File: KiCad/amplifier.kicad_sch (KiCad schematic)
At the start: 0 parts

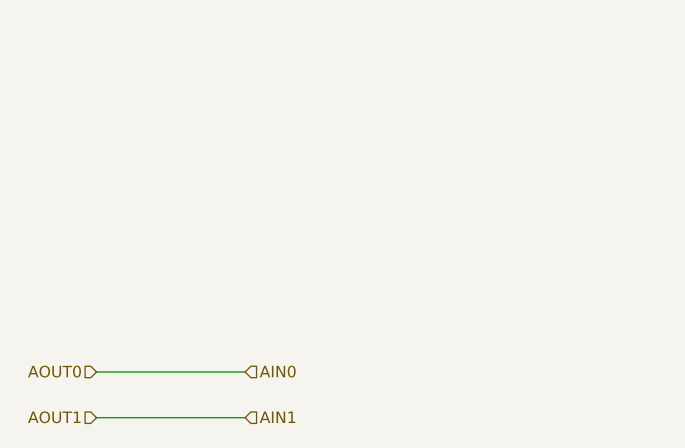
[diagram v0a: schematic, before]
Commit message: Add MCP6V92 Amplifier
Add amplifier part to amplifier block
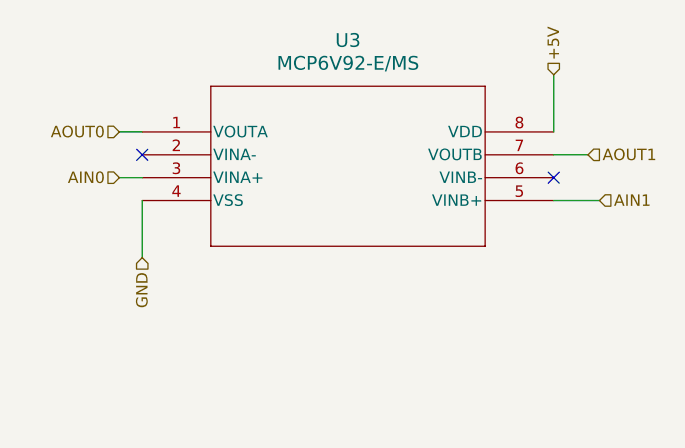
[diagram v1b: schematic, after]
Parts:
- added U3: MCP6V92-E/MS, MSOP8_MS_MCH, symbol Amplifier_Difference:MCP6V92-E_MS
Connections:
- net AIN0: now also U3.3 (VINA+)
- net AIN1: now also U3.5 (VINB+)
- new net +5V: U3.8 (VDD)
- new net AOUT0: U3.1 (VOUTA)
- new net AOUT1: U3.7 (VOUTB)
- new net GND: U3.4 (VSS)
- no-connect marks 0 -> 2
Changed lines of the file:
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@@
 	(generator_version "8.0")
 	(paper "A4")
-	(wire
-		(pts
-			(xy 102.87 95.25) (xy 119.38 95.25)
-		)
-		(stroke
-			(width 0)
-			(type default)
-		)
-	)
-	(wire
-		(pts
-			(xy 102.87 90.17) (xy 119.38 90.17)
+	(no_connect
+		(at 153.67 68.58)
+	)
+	(no_connect
+		(at 107.95 66.04)
+	)
+	(wire
+		(pts
+			(xy 107.95 77.47) (xy 107.95 71.12)
+		)
+		(stroke
+			(width 0)
+			(type default)
+		)
+	)
+	(wire
+		(pts
+			(xy 105.41 68.58) (xy 107.95 68.58)
+		)
+		(stroke
+			(width 0)
+			(type default)
+		)
+	)
+	(wire
+		(pts
+			(xy 105.41 63.5) (xy 107.95 63.5)
+		)
+		(stroke
+			(width 0)
+			(type default)
+		)
+	)
+	(wire
+		(pts
+			(xy 158.75 71.12) (xy 153.67 71.12)
+		)
+		(stroke
+			(width 0)
+			(type default)
+		)
+	)
+	(wire
+		(pts
+			(xy 153.67 57.15) (xy 153.67 63.5)
+		)
+		(stroke
+			(width 0)
+			(type default)
+		)
+	)
+	(wire
+		(pts
+			(xy 157.48 66.04) (xy 153.67 66.04)
 		)
 		(stroke
@@
 	(hierarchical_label "AIN1"
 		(shape input)
-		(at 119.38 95.25 0)
+		(at 158.75 71.12 0)
 		(fields_autoplaced yes)
 		(effects
@@
 		)
 	)
+	(hierarchical_label "+5V"
+		(shape input)
+		(at 153.67 57.15 90)
+		(fields_autoplaced yes)
+		(effects
+			(font
+				(size 1.27 1.27)
+			)
+			(justify left)
+		)
+	)
 	(hierarchical_label "AIN0"
 		(shape input)
-		(at 119.38 90.17 0)
+		(at 105.41 68.58 180)
+		(fields_autoplaced yes)
+		(effects
+			(font
+				(size 1.27 1.27)
+			)
+			(justify right)
+		)
+	)
+	(hierarchical_label "GND"
+		(shape input)
+		(at 107.95 77.47 270)
+		(fields_autoplaced yes)
+		(effects
+			(font
+				(size 1.27 1.27)
+			)
+			(justify right)
+		)
+	)
+	(hierarchical_label "AOUT0"
+		(shape input)
+		(at 105.41 63.5 180)
+		(fields_autoplaced yes)
+		(effects
+			(font
+				(size 1.27 1.27)
+			)
+			(justify right)
+		)
+	)
+	(hierarchical_label "AOUT1"
+		(shape input)
+		(at 157.48 66.04 0)
 		(fields_autoplaced yes)
 		(effects
@@
 		)
 	)
-	(hierarchical_label "AOUT0"
-		(shape input)
-		(at 102.87 90.17 180)
-		(fields_autoplaced yes)
-		(effects
-			(font
-				(size 1.27 1.27)
-			)
-			(justify right)
-		)
-	)
-	(hierarchical_label "AOUT1"
-		(shape input)
-		(at 102.87 95.25 180)
-		(fields_autoplaced yes)
-		(effects
-			(font
-				(size 1.27 1.27)
-			)
-			(justify right)
-		)
-	)
+	(symbol
+		(lib_id "Amplifier_Difference:MCP6V92-E_MS")
+		(at 107.95 63.5 0)
+		(unit 1)
+		(exclude_from_sim no)
+		(in_bom yes)
+		(on_board yes)
+		(dnp no)
+		(fields_autoplaced yes)
+		(property "Reference" "U3"
+			(at 130.81 53.34 0)
+			(effects
+				(font
+					(size 1.524 1.524)
+				)
+			)
+		)
+		(property "Value" "MCP6V92-E/MS"
+			(at 130.81 55.88 0)
+			(effects
+				(font
+					(size 1.524 1.524)
+				)
+			)
+		)
+		(property "Footprint" "MSOP8_MS_MCH"
+			(at 107.95 63.5 0)
+			(effects
+				(font
+					(size 1.27 1.27)
+					(italic yes)
+				)
+				(hide yes)
+			)
+		)
+		(property "Datasheet" "MCP6V92-E/MS"
+			(at 107.95 63.5 0)
+			(effects
+				(font
+					(size 1.27 1.27)
+					(italic yes)
+				)
+				(hide yes)
+			)
+		)
+		(property "Description" ""
+			(at 107.95 63.5 0)
+			(effects
+				(font
+					(size 1.27 1.27)
+				)
+				(hide yes)
+			)
+		)
+		(pin "1"
+		)
+		(pin "5"
+		)
+		(pin "6"
+		)
+		(pin "2"
+		)
+		(pin "7"
+		)
+		(pin "8"
+		)
+		(pin "3"
+		)
+		(pin "4"
+		)
+		(instances
+			(project ""
+				(path "/5d164854-6659-4076-ba4e-df0771b4723d/0ca0ce53-f671-4079-bef4-c51bb5c4b2f4"
+					(reference "U3")
+					(unit 1)
+				)
+			)
+		)
+	)

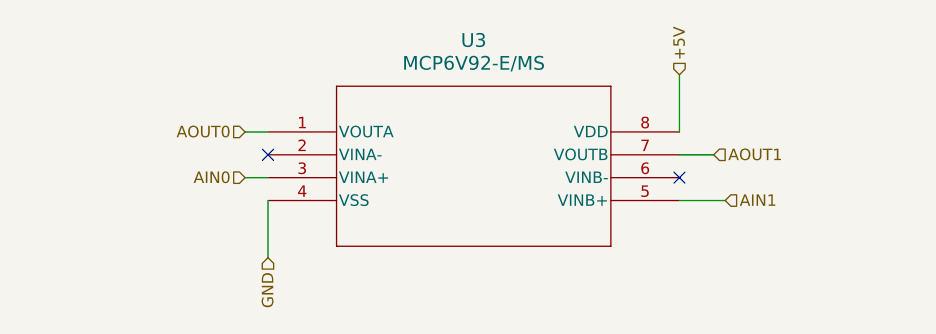
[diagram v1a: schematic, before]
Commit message: Add bypass resistors for Amplifier
Add 0R resistor pads to allow the amplifier to be bypassed so we can test with/without it in the circuit.
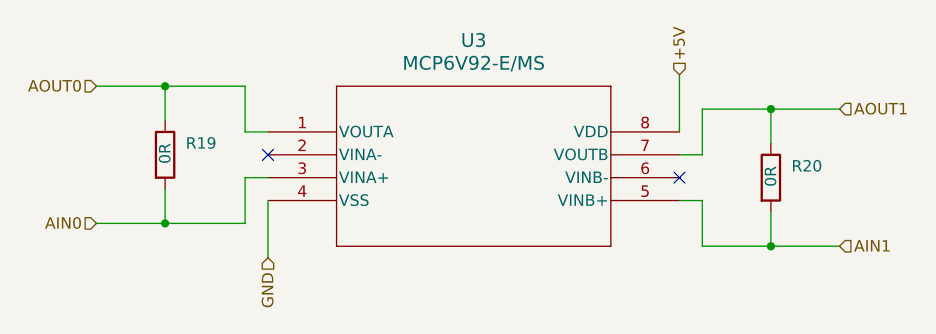
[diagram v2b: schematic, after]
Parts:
- added R19, R20: 0R, symbol Device:R
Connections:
- net AIN0: now also R19.2
- net AIN1: now also R20.2
- net AOUT0: now also R19.1
- net AOUT1: now also R20.1

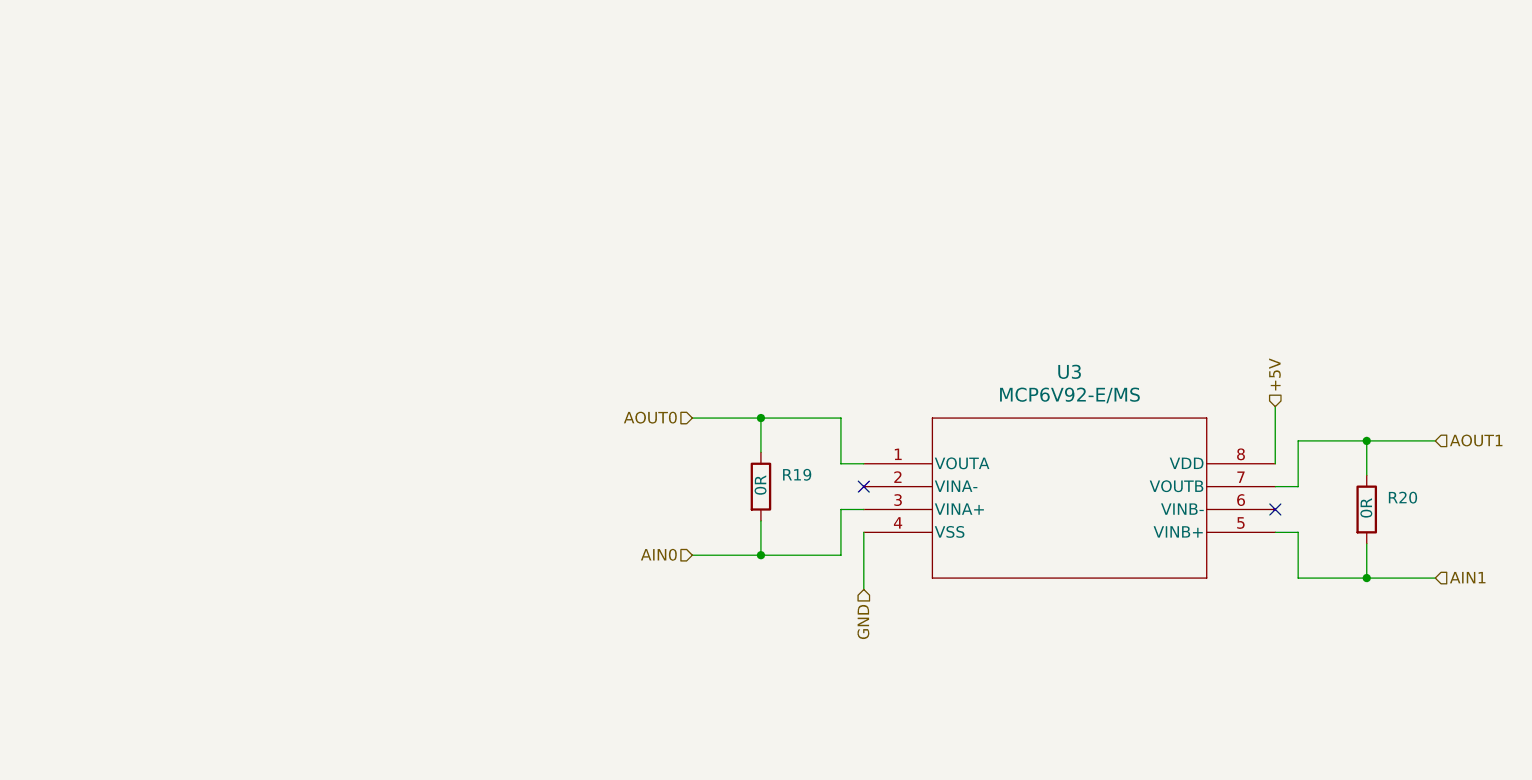
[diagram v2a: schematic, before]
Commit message: Use 12V Power
* Use 12 V Power
* Update to an F103 processor with better compatibility with Katapult
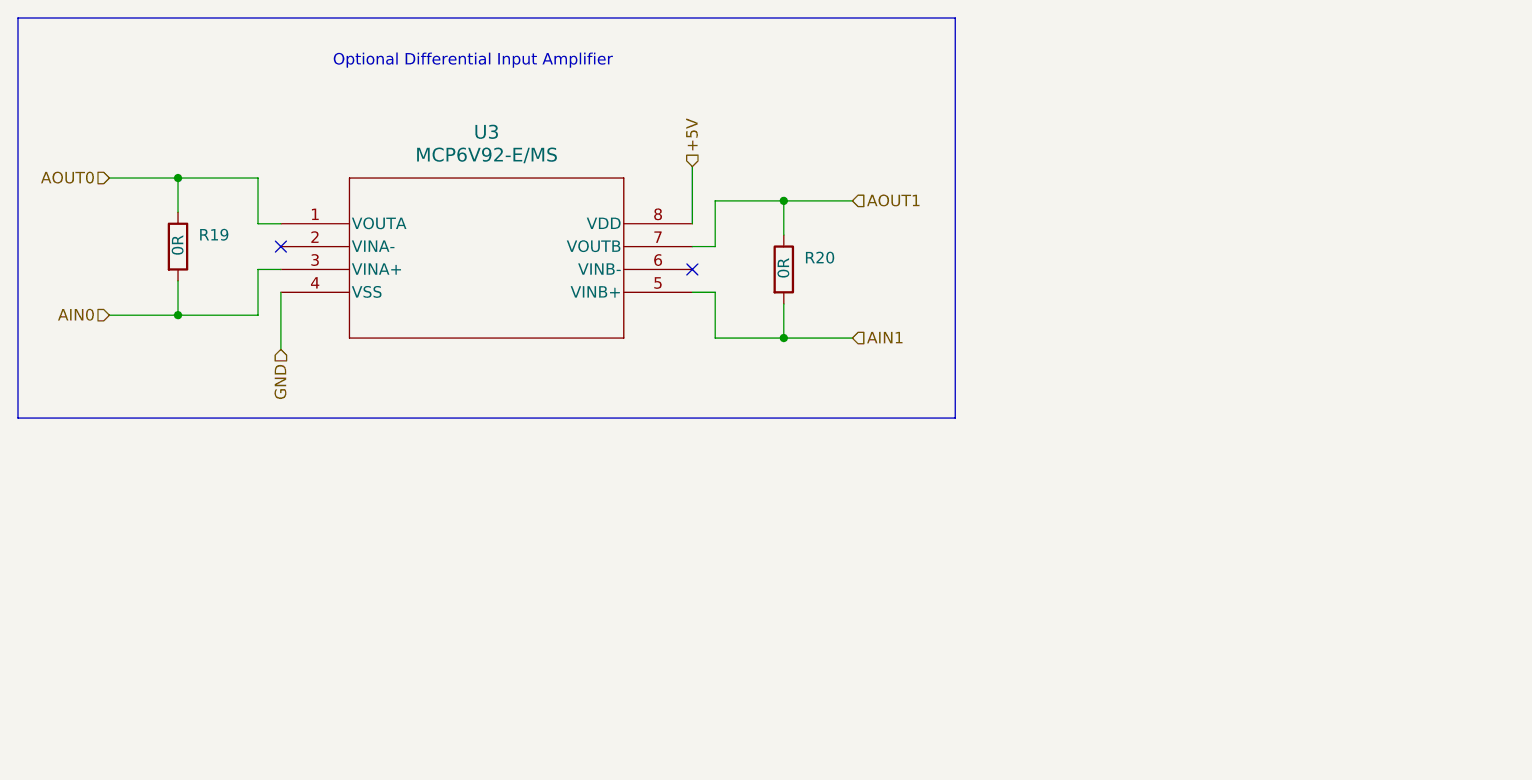
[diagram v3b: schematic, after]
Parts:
- R19, R20: footprint (none) -> Capacitor_SMD:C_0603_1608Metric_Pad1.08x0.95mm_HandSolder
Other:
- note added: "Optional Differential Input Amplifier"
- moved on the sheet: R19, R20, U3

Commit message: Update 5V Power Stage
* Update the 5V power stage based on the recommendations from TI.
* Updated standard passive footprint to 0805 hand solder configuration
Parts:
- R19, R20: footprint Capacitor_SMD:C_0603_1608Metric_Pad1.08x0.95mm_HandSolder -> Resistor_SMD:R_0805_2012Metric_Pad1.20x1.40mm_HandSolder
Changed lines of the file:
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@@
 			)
 		)
-		(property "Footprint" "Capacitor_SMD:C_0603_1608Metric_Pad1.08x0.95mm_HandSolder"
+		(property "Footprint" "Resistor_SMD:R_0805_2012Metric_Pad1.20x1.40mm_HandSolder"
 			(at 29.972 39.37 90)
 			(effects
@@
 			)
 		)
-		(property "Footprint" "Capacitor_SMD:C_0603_1608Metric_Pad1.08x0.95mm_HandSolder"
+		(property "Footprint" "Resistor_SMD:R_0805_2012Metric_Pad1.20x1.40mm_HandSolder"
 			(at 97.282 41.91 90)
 			(effects

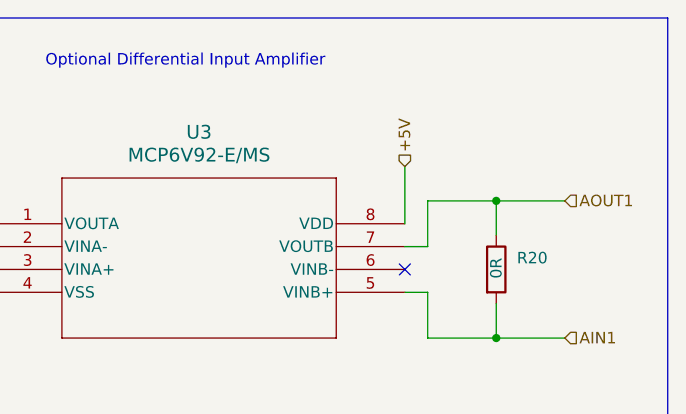
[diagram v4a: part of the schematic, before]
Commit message: Convert Power to LDOs
Convert power section to use only LDOs. This means we will only get 4.75V or 4.5V on the analog line but this comes with greatly increased simplicity of layout.
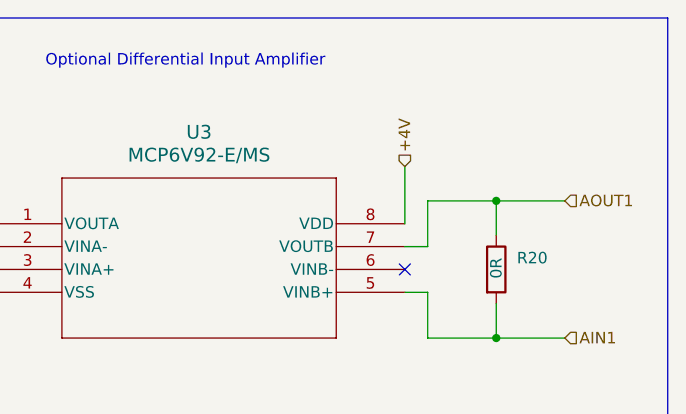
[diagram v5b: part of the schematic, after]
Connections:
- net +5V renamed +4V
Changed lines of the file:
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@@
 		)
 	)
-	(hierarchical_label "+5V"
+	(hierarchical_label "+4V"
 		(shape input)
 		(at 88.9 30.48 90)

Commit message: Work In Progress
moving towards v 2
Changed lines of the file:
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@@
 		(dnp no)
 		(property "Reference" "R19"
-			(at 34.036 38.1 0)
+			(at 33.782 39.37 0)
 			(effects
 				(font
